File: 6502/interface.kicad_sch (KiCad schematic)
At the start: 18 parts, among them J1 Conn_02x20_Odd_Even, J11 Mini-DIN-6, J12 Jack-DC, J13 Conn_01x02, J15 Conn_01x02, J17 Conn_01x02, J2 Conn_02x20_Odd_Even, J3 Conn_01x08, J4 Conn_01x08, J5 Conn_01x03, J6 Conn_02x20_Odd_Even, J7 Conn_02x20_Odd_Even, J8 Conn_01x05, J9 Conn_01x08, Q1 FQP47P06, U13 LM7805_TO220

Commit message: pcb almost done
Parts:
- C12: renamed from C17; footprint Capacitor_THT:C_Disc_D5.1mm_W3.2mm_P5.00mm -> Capacitor_THT:C_Radial_D5.0mm_H11.0mm_P2.00mm
- C13: renamed from C18; footprint Capacitor_THT:C_Disc_D5.1mm_W3.2mm_P5.00mm -> Capacitor_THT:C_Radial_D5.0mm_H11.0mm_P2.00mm
- J5: renamed from J9; footprint Connector_PinHeader_2.54mm:PinHeader_1x05_P2.54mm_Vertical -> Connector_PinHeader_2.54mm:PinHeader_1x08_P2.54mm_Vertical
- renumbered J3 to J1, J6 to J10, J7 to J12, J12 to J13, J17 to J14, J4 to J2, J5 to J3, J1 to J4, J8 to J6, J2 to J7, J15 to J8, J13 to J9, U13 to U10
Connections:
- net 1CB1: now also J5.2 (Pin_2); no longer J5.1 (Pin_1)
- net 1CB2: now also J5.1 (Pin_1); no longer J5.2 (Pin_2)

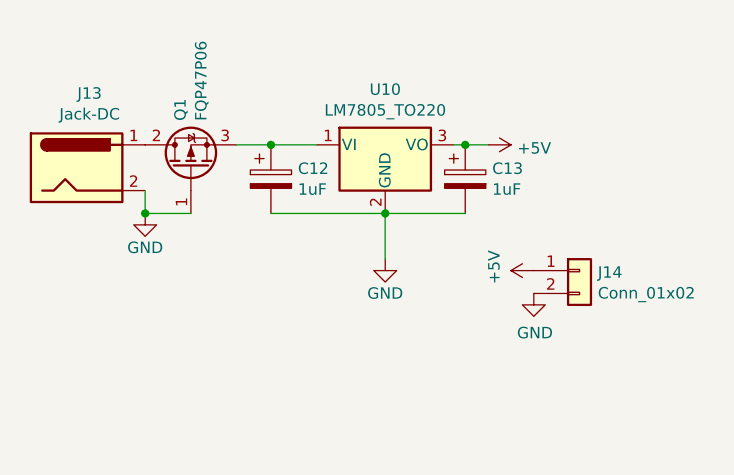
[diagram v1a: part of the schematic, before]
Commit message: fixed decoder circuit
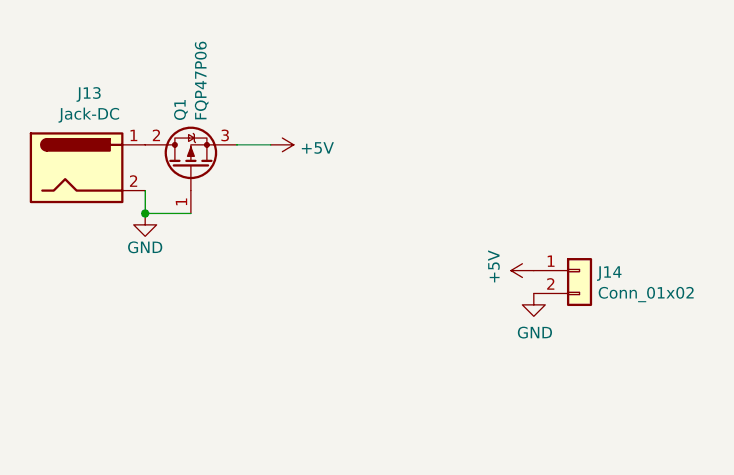
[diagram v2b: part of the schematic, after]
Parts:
- removed C12, C13: 1uF, Capacitor_THT:C_Radial_D5.0mm_H11.0mm_P2.00mm, symbol Device:CP
- removed U10: LM7805_TO220, Package_TO_SOT_THT:TO-251-3-1EP_Horizontal_TabDown, symbol Regulator_Linear:LM7805_TO220
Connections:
- net +5V: now also Q1.3 (S)
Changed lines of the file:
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@@
     (rev "1.1")
-  )
-  (junction (at 241.3 36.83) (diameter 0) (color 0 0 0 0)
-  )
-  (junction (at 250.19 29.21) (diameter 0) (color 0 0 0 0)
-  )
-  (junction (at 228.6 29.21) (diameter 0) (color 0 0 0 0)
   )
   (junction (at 214.63 36.83) (diameter 0) (color 0 0 0 0)
@@
     (stroke (width 0) (type default) (color 0 0 0 0))
   )
-  (wire (pts (xy 241.3 36.83) (xy 241.3 41.91))
-    (stroke (width 0) (type default) (color 0 0 0 0))
-  )
   (bus (pts (xy 177.8 110.49) (xy 177.8 113.03))
     (stroke (width 0) (type default) (color 0 0 0 0))
@@
     (stroke (width 0) (type default) (color 0 0 0 0))
   )
-  (wire (pts (xy 228.6 36.83) (xy 241.3 36.83))
-    (stroke (width 0) (type default) (color 0 0 0 0))
-  )
   (bus (pts (xy 130.81 100.33) (xy 130.81 102.87))
     (stroke (width 0) (type default) (color 0 0 0 0))
@@
     (stroke (width 0) (type default) (color 0 0 0 0))
   )
-  (wire (pts (xy 228.6 29.21) (xy 233.68 29.21))
-    (stroke (width 0) (type default) (color 0 0 0 0))
-  )
   (wire (pts (xy 139.7 133.35) (xy 133.35 133.35))
     (stroke (width 0) (type default) (color 0 0 0 0))
@@
     (stroke (width 0) (type default) (color 0 0 0 0))
   )
-  (wire (pts (xy 250.19 29.21) (xy 252.73 29.21))
-    (stroke (width 0) (type default) (color 0 0 0 0))
-  )
   (bus (pts (xy 111.76 90.17) (xy 111.76 92.71))
     (stroke (width 0) (type default) (color 0 0 0 0))
@@
     (stroke (width 0) (type default) (color 0 0 0 0))
   )
-  (wire (pts (xy 248.92 29.21) (xy 250.19 29.21))
-    (stroke (width 0) (type default) (color 0 0 0 0))
-  )
   (wire (pts (xy 104.14 100.33) (xy 109.22 100.33))
     (stroke (width 0) (type default) (color 0 0 0 0))
@@
   )
   (wire (pts (xy 133.35 123.19) (xy 139.7 123.19))
-    (stroke (width 0) (type default) (color 0 0 0 0))
-  )
-  (wire (pts (xy 241.3 36.83) (xy 250.19 36.83))
     (stroke (width 0) (type default) (color 0 0 0 0))
   )
@@
   (symbol (lib_id "power:+5V") (at 160.02 40.64 90) (unit 1)
     (in_bom yes) (on_board yes)
-    (property "Reference" "#PWR048" (id 0) (at 163.83 40.64 0)
+    (property "Reference" "#PWR049" (id 0) (at 163.83 40.64 0)
       (effects (font (size 1.27 1.27)) hide)
     )
@@
   (symbol (lib_id "power:GND") (at 214.63 36.83 0) (unit 1)
     (in_bom yes) (on_board yes)
-    (property "Reference" "#PWR052" (id 0) (at 214.63 43.18 0)
+    (property "Reference" "#PWR053" (id 0) (at 214.63 43.18 0)
       (effects (font (size 1.27 1.27)) hide)
     )
@@
     (pin "3")
   )
-  (symbol (lib_id "Regulator_Linear:LM7805_TO220") (at 241.3 29.21 0) (unit 1)
-    (in_bom yes) (on_board yes)
-    (property "Reference" "U10" (id 0) (at 241.3 23.0632 0))
-    (property "Value" "LM7805_TO220" (id 1) (at 241.3 25.3746 0))
-    (property "Footprint" "Package_TO_SOT_THT:TO-251-3-1EP_Horizontal_TabDown" (id 2) (at 241.3 23.495 0)
-      (effects (font (size 1.27 1.27) italic) hide)
-    )
-    (property "Datasheet" "https://www.onsemi.cn/PowerSolutions/document/MC7800-D.PDF" (id 3) (at 241.3 30.48 0)
-      (effects (font (size 1.27 1.27)) hide)
-    )
-    (pin "1")
-    (pin "2")
-    (pin "3")
-  )
-  (symbol (lib_id "power:GND") (at 241.3 41.91 0) (unit 1)
-    (in_bom yes) (on_board yes)
-    (property "Reference" "#PWR053" (id 0) (at 241.3 48.26 0)
-      (effects (font (size 1.27 1.27)) hide)
-    )
-    (property "Value" "GND" (id 1) (at 241.3 45.72 0))
-    (property "Footprint" "" (id 2) (at 241.3 41.91 0)
-      (effects (font (size 1.27 1.27)) hide)
-    )
-    (property "Datasheet" "" (id 3) (at 241.3 41.91 0)
-      (effects (font (size 1.27 1.27)) hide)
-    )
-    (pin "1")
-  )
-  (symbol (lib_id "power:+5V") (at 252.73 29.21 270) (unit 1)
-    (in_bom yes) (on_board yes)
-    (property "Reference" "#PWR054" (id 0) (at 248.92 29.21 0)
-      (effects (font (size 1.27 1.27)) hide)
-    )
-    (property "Value" "+5V" (id 1) (at 255.9812 29.591 90)
+  (symbol (lib_id "power:+5V") (at 228.6 29.21 270) (unit 1)
+    (in_bom yes) (on_board yes)
+    (property "Reference" "#PWR054" (id 0) (at 224.79 29.21 0)
+      (effects (font (size 1.27 1.27)) hide)
+    )
+    (property "Value" "+5V" (id 1) (at 231.8512 29.591 90)
       (effects (font (size 1.27 1.27)) (justify left))
     )
-    (property "Footprint" "" (id 2) (at 252.73 29.21 0)
-      (effects (font (size 1.27 1.27)) hide)
-    )
-    (property "Datasheet" "" (id 3) (at 252.73 29.21 0)
+    (property "Footprint" "" (id 2) (at 228.6 29.21 0)
+      (effects (font (size 1.27 1.27)) hide)
+    )
+    (property "Datasheet" "" (id 3) (at 228.6 29.21 0)
       (effects (font (size 1.27 1.27)) hide)
     )
@@
   (symbol (lib_id "power:+5V") (at 91.44 135.89 90) (unit 1)
     (in_bom yes) (on_board yes)
-    (property "Reference" "#PWR044" (id 0) (at 95.25 135.89 0)
+    (property "Reference" "#PWR045" (id 0) (at 95.25 135.89 0)
       (effects (font (size 1.27 1.27)) hide)
     )
@@
   (symbol (lib_id "power:GND") (at 104.14 135.89 0) (unit 1)
     (in_bom yes) (on_board yes)
-    (property "Reference" "#PWR045" (id 0) (at 104.14 142.24 0)
+    (property "Reference" "#PWR046" (id 0) (at 104.14 142.24 0)
       (effects (font (size 1.27 1.27)) hide)
     )
@@
   (symbol (lib_id "power:+5V") (at 139.7 135.89 90) (unit 1)
     (in_bom yes) (on_board yes)
-    (property "Reference" "#PWR046" (id 0) (at 143.51 135.89 0)
+    (property "Reference" "#PWR047" (id 0) (at 143.51 135.89 0)
       (effects (font (size 1.27 1.27)) hide)
     )
@@
   (symbol (lib_id "power:GND") (at 152.4 135.89 0) (unit 1)
     (in_bom yes) (on_board yes)
-    (property "Reference" "#PWR047" (id 0) (at 152.4 142.24 0)
+    (property "Reference" "#PWR048" (id 0) (at 152.4 142.24 0)
       (effects (font (size 1.27 1.27)) hide)
     )
@@
   (symbol (lib_id "power:+5V") (at 186.69 135.89 90) (unit 1)
     (in_bom yes) (on_board yes)
-    (property "Reference" "#PWR050" (id 0) (at 190.5 135.89 0)
+    (property "Reference" "#PWR051" (id 0) (at 190.5 135.89 0)
       (effects (font (size 1.27 1.27)) hide)
     )
@@
   (symbol (lib_id "power:GND") (at 199.39 135.89 0) (unit 1)
     (in_bom yes) (on_board yes)
-    (property "Reference" "#PWR051" (id 0) (at 199.39 142.24 0)
+    (property "Reference" "#PWR052" (id 0) (at 199.39 142.24 0)
       (effects (font (size 1.27 1.27)) hide)
     )
@@
     (pin "2")
   )
-  (symbol (lib_id "Device:CP") (at 250.19 33.02 0) (unit 1)
-    (in_bom yes) (on_board yes)
-    (property "Reference" "C13" (id 0) (at 253.1872 31.8516 0)
-      (effects (font (size 1.27 1.27)) (justify left))
-    )
-    (property "Value" "1uF" (id 1) (at 253.1872 34.163 0)
-      (effects (font (size 1.27 1.27)) (justify left))
-    )
-    (property "Footprint" "Capacitor_THT:C_Radial_D5.0mm_H11.0mm_P2.00mm" (id 2) (at 251.1552 36.83 0)
-      (effects (font (size 1.27 1.27)) hide)
-    )
-    (property "Datasheet" "~" (id 3) (at 250.19 33.02 0)
-      (effects (font (size 1.27 1.27)) hide)
-    )
-    (pin "1")
-    (pin "2")
-  )
-  (symbol (lib_id "Device:CP") (at 228.6 33.02 0) (unit 1)
-    (in_bom yes) (on_board yes)
-    (property "Reference" "C12" (id 0) (at 231.5972 31.8516 0)
-      (effects (font (size 1.27 1.27)) (justify left))
-    )
-    (property "Value" "1uF" (id 1) (at 231.5972 34.163 0)
-      (effects (font (size 1.27 1.27)) (justify left))
-    )
-    (property "Footprint" "Capacitor_THT:C_Radial_D5.0mm_H11.0mm_P2.00mm" (id 2) (at 229.5652 36.83 0)
-      (effects (font (size 1.27 1.27)) hide)
-    )
-    (property "Datasheet" "~" (id 3) (at 228.6 33.02 0)
-      (effects (font (size 1.27 1.27)) hide)
-    )
-    (pin "1")
-    (pin "2")
-  )
   (symbol (lib_id "power:GND") (at 54.61 135.89 0) (unit 1)
     (in_bom yes) (on_board yes)
-    (property "Reference" "#PWR043" (id 0) (at 54.61 142.24 0)
+    (property "Reference" "#PWR044" (id 0) (at 54.61 142.24 0)
       (effects (font (size 1.27 1.27)) hide)
     )
@@
   (symbol (lib_id "power:GND") (at 179.07 45.72 0) (unit 1)
     (in_bom yes) (on_board yes)
-    (property "Reference" "#PWR049" (id 0) (at 179.07 52.07 0)
+    (property "Reference" "#PWR050" (id 0) (at 179.07 52.07 0)
       (effects (font (size 1.27 1.27)) hide)
     )
@@
   (symbol (lib_id "power:+5V") (at 41.91 135.89 90) (unit 1)
     (in_bom yes) (on_board yes)
-    (property "Reference" "#PWR042" (id 0) (at 45.72 135.89 0)
-      (effects (font (size 1.27 1.27)) hide)
-    )
+    (property "Reference" "#PWR043" (id 0) (at 45.72 135.89 0)
+      (effects (font (size 1.27 1.27)) hide)
+    )

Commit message: updated pcb
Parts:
- removed J6: Conn_01x05, Connector_PinHeader_2.54mm:PinHeader_1x05_P2.54mm_Vertical, symbol Connector_Generic:Conn_01x05
- removed J8, J9: Conn_01x02, Connector_PinHeader_2.54mm:PinHeader_1x02_P2.54mm_Vertical, symbol Connector_Generic:Conn_01x02
- added J6: Conn_01x03, Connector_PinHeader_2.54mm:PinHeader_1x03_P2.54mm_Vertical, symbol Connector_Generic:Conn_01x03
- renumbered J12 to J10, J13 to J11, J14 to J12, J10 to J8, J11 to J9
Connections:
- net PHI1O is gone; now on net +5V: J10.38 (Pin_38), J4.38 (Pin_38), J7.38 (Pin_38), J8.38 (Pin_38)
- net +5V: no longer J10.39 (Pin_39), J4.39 (Pin_39), J7.39 (Pin_39), J8.39 (Pin_39)
- net decode0: now also J6.1 (Pin_1)
- net decode1: now also J6.2 (Pin_2)
- net decode2: now also J6.3 (Pin_3)
- net dev10 renamed IO8
- net dev11 renamed IO9
- net dev12 renamed IO10
- net dev13 renamed IO12
- net dev14 renamed IO13
- net dev15 renamed IO14
- net dev4 renamed IO0
- net dev5 renamed IO1
- net dev6 renamed IO2
- net dev7 renamed IO4
- net dev8 renamed IO5
- net dev9 renamed IO6
- new net IO11: J8.39 (Pin_39)
- new net IO15: J10.39 (Pin_39)
- new net IO3: J4.39 (Pin_39)
- new net IO7: J7.39 (Pin_39)
